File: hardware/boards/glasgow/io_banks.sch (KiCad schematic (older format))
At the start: 21 parts, among them J10 Conn_01x03, J4 Conn_01x02, J5 Conn_02x22_Odd_Even, U30 ICE40HX8K-BG121, U32 SN74LVC1T45DRL

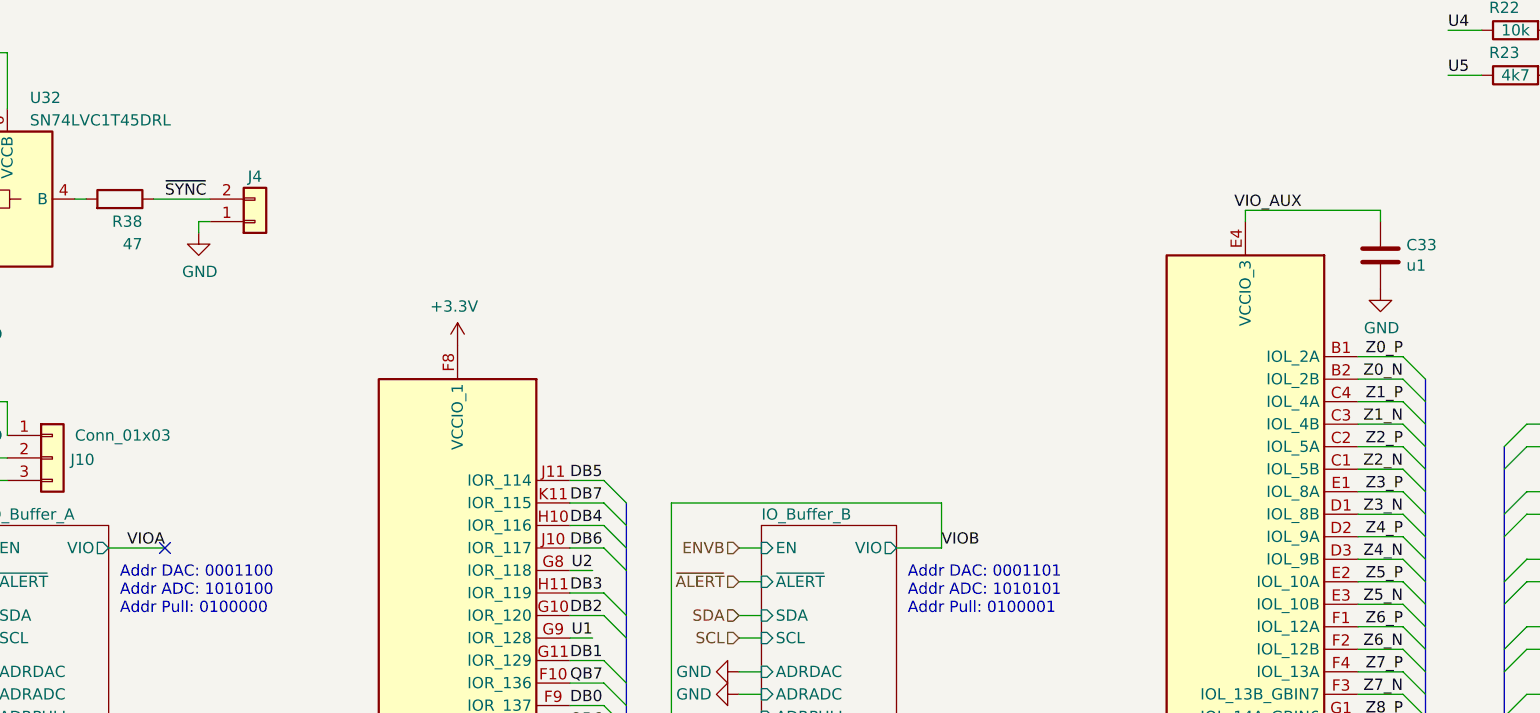
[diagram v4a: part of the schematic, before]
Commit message: revC1: fix some ERC errors
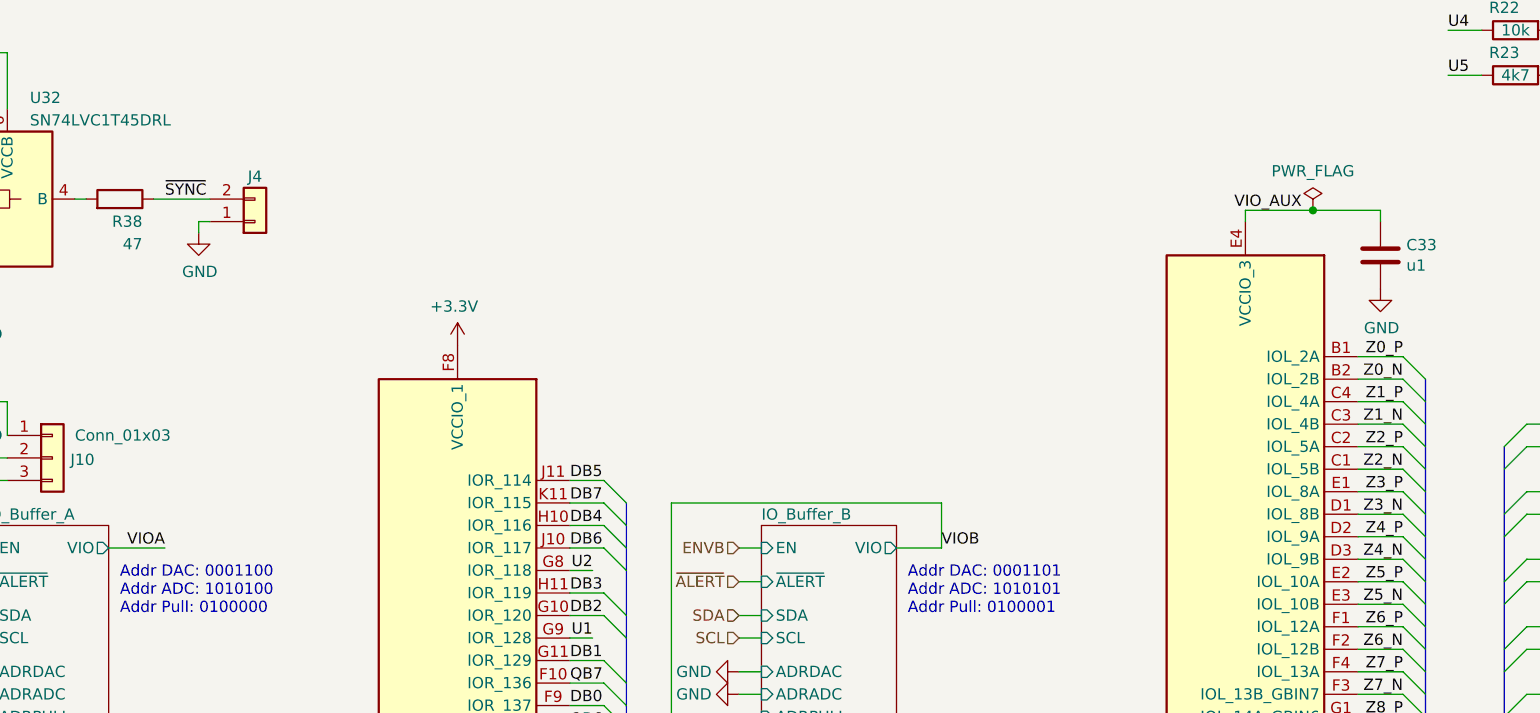
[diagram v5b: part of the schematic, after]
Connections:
- no-connect marks 3 -> 2
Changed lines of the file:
@@
 Text Label 3450 3950 2    50   ~ 0
 VIOA
-NoConn ~ 3450 3950
 Wire Wire Line
 	3200 3950 3450 3950
@@
 $EndComp
 Wire Wire Line
-	8250 2450 8850 2450
+	8250 2450 8550 2450
 Connection ~ 2400 5800
 Connection ~ 5850 5800
@@
 Wire Bus Line
 	9050 3200 9050 5800
+$Comp
+L power:PWR_FLAG #FLG0101
+U 1 1 5CFF6FB6
+P 8550 2450
+F 0 "#FLG0101" H 8550 2525 50  0001 C CNN
+F 1 "PWR_FLAG" H 8550 2624 50  0000 C CNN
+F 2 "" H 8550 2450 50  0001 C CNN
+F 3 "~" H 8550 2450 50  0001 C CNN
+	1    8550 2450
+	1    0    0    -1
+$EndComp
+Connection ~ 8550 2450
+Wire Wire Line
+	8550 2450 8850 2450
 $EndSCHEMATC

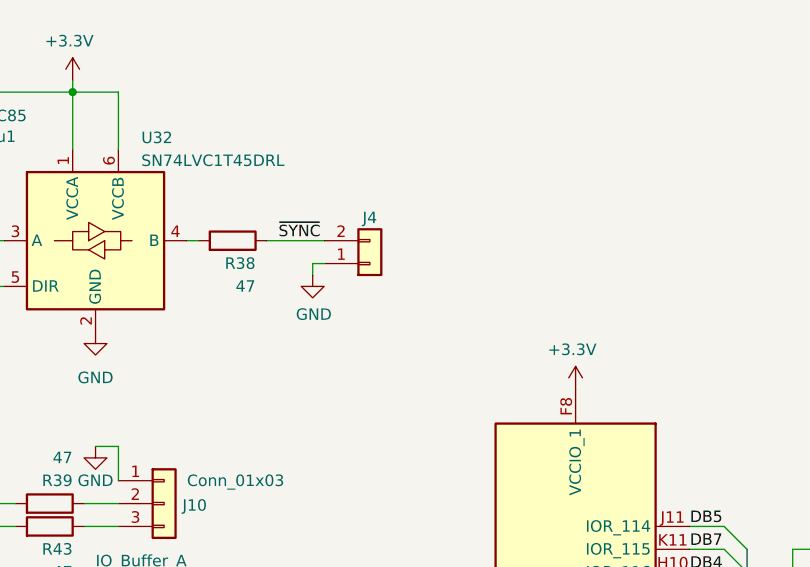
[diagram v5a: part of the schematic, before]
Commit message: revC1: add a TVS protection diode to SYNC
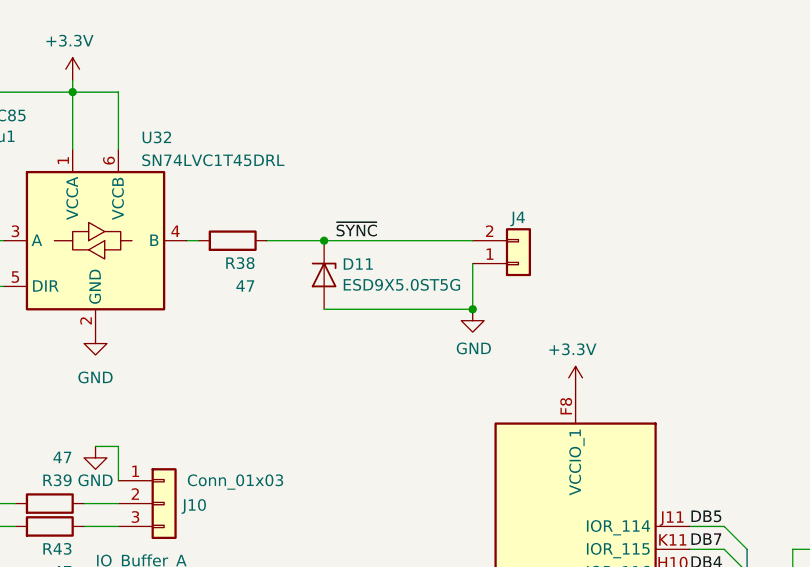
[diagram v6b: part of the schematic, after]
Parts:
- added D11: ESD9X5.0ST5G, Diode_SMD:D_0402_1005Metric, symbol Device:D_Zener
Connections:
- net GND: now also D11.2 (A)
- net ~SYNC: now also D11.1 (K)
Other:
- moved on the sheet: J4
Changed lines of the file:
@@
 L Connector_Generic:Conn_01x02 J?
 U 1 1 5C961091
-P 3850 2500
+P 4500 2500
 AR Path="/5C961091" Ref="J?"  Part="1"
 AR Path="/5C7B59B0/5C961091" Ref="J4"  Part="1"
-F 0 "J4" H 3850 2300 50  0000 C CNN
-F 1 "Conn_01x02" H 3930 2401 50  0001 L CNN
-F 2 "Connector_PinHeader_2.54mm:PinHeader_1x02_P2.54mm_Horizontal" H 3850 2500 50  0001 C CNN
-F 3 "https://www.mouser.hk/datasheet/2/418/NG_CD_640455_Y3-1255934.pdf" H 3850 2500 50  0001 C CNN
-F 4 "Molex" H -6750 -350 50  0001 C CNN "Mfg"
-F 5 "22-05-3021" H -6750 -350 50  0001 C CNN "MPN"
-	1    3850 2500
+F 0 "J4" H 4500 2300 50  0000 C CNN
+F 1 "Conn_01x02" H 4580 2401 50  0001 L CNN
+F 2 "Connector_PinHeader_2.54mm:PinHeader_1x02_P2.54mm_Horizontal" H 4500 2500 50  0001 C CNN
+F 3 "https://www.mouser.hk/datasheet/2/418/NG_CD_640455_Y3-1255934.pdf" H 4500 2500 50  0001 C CNN
+F 4 "Molex" H -6100 -350 50  0001 C CNN "Mfg"
+F 5 "22-05-3021" H -6100 -350 50  0001 C CNN "MPN"
+	1    4500 2500
 	1    0    0    1
 $EndComp
@@
 L power:GND #PWR?
 U 1 1 5C961098
-P 3600 2550
+P 4300 2700
 AR Path="/5C961098" Ref="#PWR?"  Part="1"
 AR Path="/5C7B59B0/5C961098" Ref="#PWR042"  Part="1"
-F 0 "#PWR042" H 3600 2300 50  0001 C CNN
-F 1 "GND" H 3605 2377 50  0000 C CNN
-F 2 "" H 3600 2550 50  0001 C CNN
-F 3 "" H 3600 2550 50  0001 C CNN
-	1    3600 2550
-	1    0    0    -1
-$EndComp
-Wire Wire Line
-	3650 2500 3600 2500
-Wire Wire Line
-	3600 2500 3600 2550
-Text Label 3450 2400 0    50   ~ 0
+F 0 "#PWR042" H 4300 2450 50  0001 C CNN
+F 1 "GND" H 4305 2527 50  0000 C CNN
+F 2 "" H 4300 2700 50  0001 C CNN
+F 3 "" H 4300 2700 50  0001 C CNN
+	1    4300 2700
+	1    0    0    -1
+$EndComp
+Text Label 3700 2400 0    50   ~ 0
 ~SYNC
 $Comp
@@
 Wire Wire Line
 	2750 3300 2750 3450
-Wire Bus Line
-	2400 4950 2400 5800
-Wire Bus Line
-	3450 4950 3450 5800
-Wire Bus Line
-	6950 4950 6950 5800
-Wire Bus Line
-	5850 4950 5850 5800
-Wire Bus Line
-	10650 3700 10650 5800
-Wire Bus Line
-	9400 3500 9400 5800
-Wire Bus Line
-	2050 3850 2050 5800
-Wire Bus Line
-	5500 3750 5500 5800
-Wire Bus Line
-	9050 3200 9050 5800
 $Comp
 L power:PWR_FLAG #FLG0101
@@
 Wire Wire Line
 	8550 2450 8850 2450
+$Comp
+L Device:D_Zener D11
+U 1 1 5D1DFDD1
+P 3650 2550
+F 0 "D11" V 3604 2629 50  0000 L CNN
+F 1 "ESD9X5.0ST5G" V 3695 2629 50  0000 L CNN
+F 2 "Diode_SMD:D_0402_1005Metric" H 3650 2550 50  0001 C CNN
+F 3 "https://www.onsemi.com/pub/Collateral/ESD9X3.3ST5G-D.PDF" H 3650 2550 50  0001 C CNN
+	1    3650 2550
+	0    1    1    0
+$EndComp
+Connection ~ 3650 2400
+Wire Wire Line
+	4300 2500 4300 2700
+Connection ~ 4300 2700
+Wire Wire Line
+	3650 2400 4300 2400
+Wire Wire Line
+	3650 2700 4300 2700
+Wire Bus Line
+	2400 4950 2400 5800
+Wire Bus Line
+	3450 4950 3450 5800
+Wire Bus Line
+	6950 4950 6950 5800
+Wire Bus Line
+	5850 4950 5850 5800
+Wire Bus Line
+	10650 3700 10650 5800
+Wire Bus Line
+	9400 3500 9400 5800
+Wire Bus Line
+	2050 3850 2050 5800
+Wire Bus Line
+	5500 3750 5500 5800
+Wire Bus Line
+	9050 3200 9050 5800
 $EndSCHEMATC

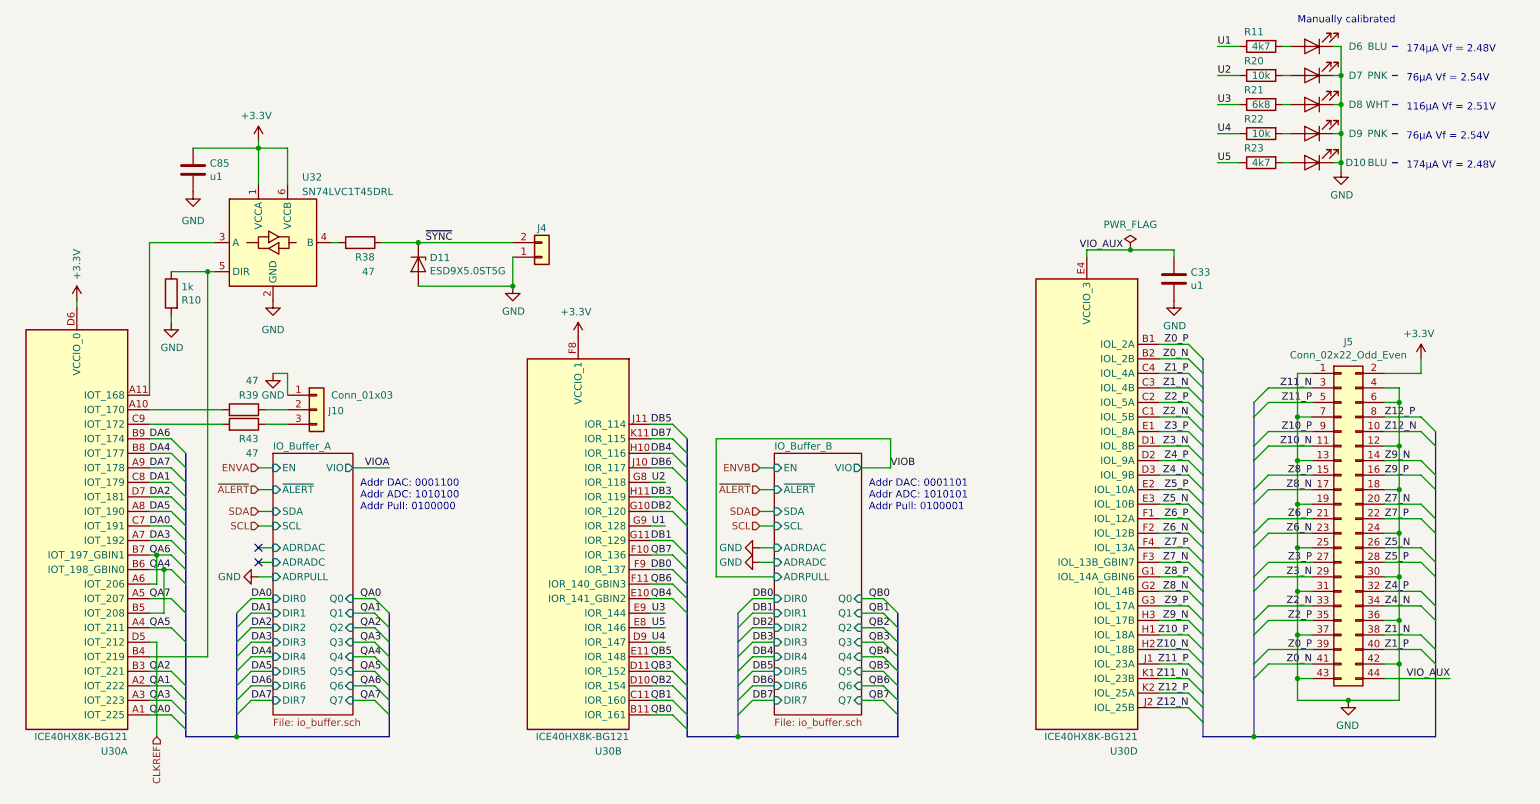
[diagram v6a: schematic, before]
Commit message: revC: tiny changes to text placement on schematic for readability.
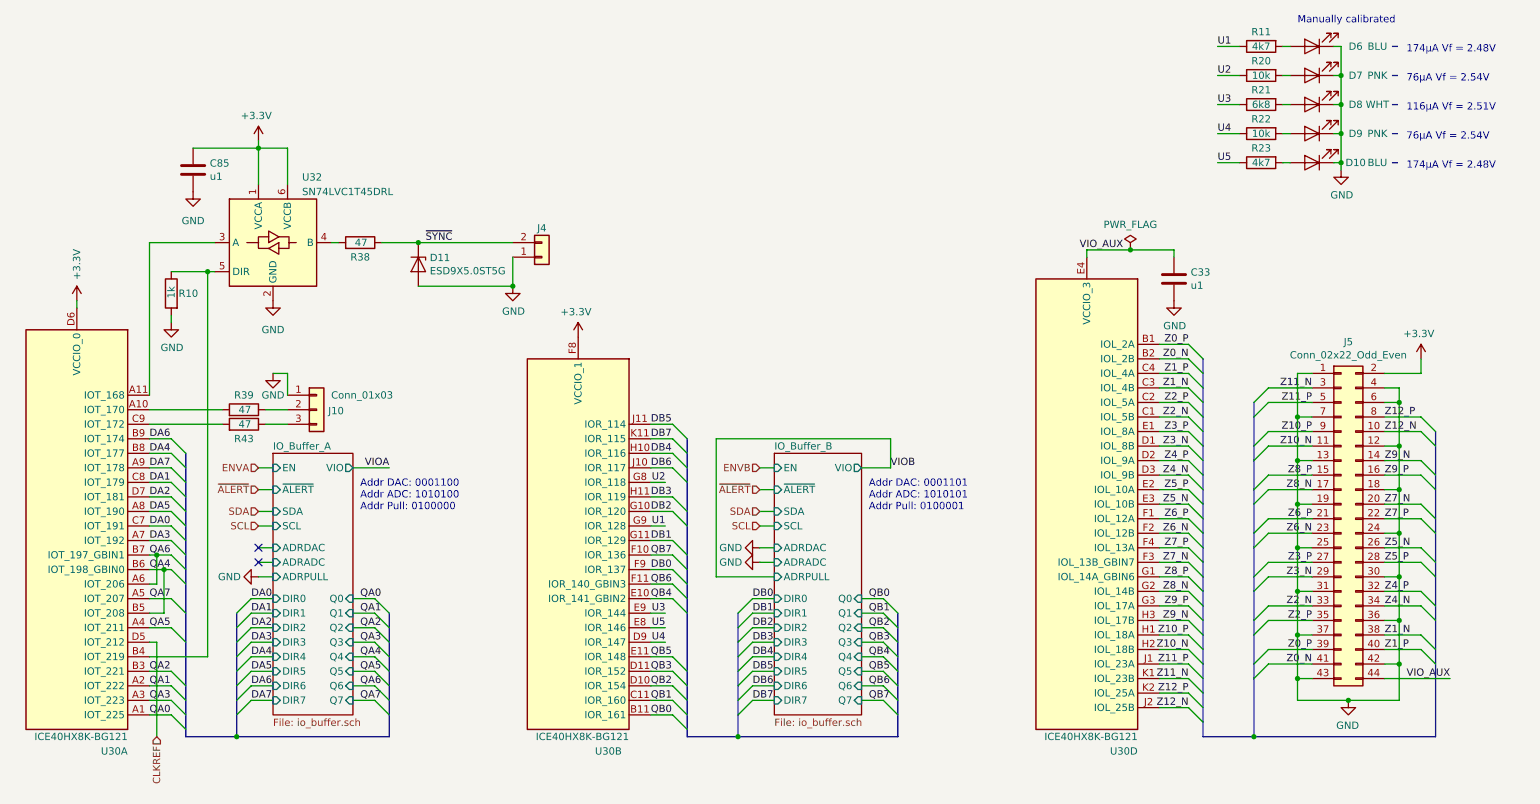
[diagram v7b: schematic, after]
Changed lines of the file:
@@
 EESchema Schematic File Version 4
 LIBS:glasgow-cache
-EELAYER 26 0
+EELAYER 29 0
 EELAYER END
 $Descr A4 11693 8268
@@
 AR Path="/5C9E34D0" Ref="R?"  Part="1"
 AR Path="/5C7B59B0/5C9E34D0" Ref="R11"  Part="1"
-F 0 "R11" V 9350 1100 50  0000 C CNN
+F 0 "R11" V 9350 1050 50  0000 C CNN
 F 1 "4k7" V 9450 1050 50  0000 C CNN
 F 2 "Resistor_SMD:R_0402_1005Metric" V 9380 1050 50  0001 C CNN
@@
 AR Path="/5C9E34DB" Ref="R?"  Part="1"
 AR Path="/5C7B59B0/5C9E34DB" Ref="R22"  Part="1"
-F 0 "R22" V 9350 1700 50  0000 C CNN
+F 0 "R22" V 9350 1650 50  0000 C CNN
 F 1 "10k" V 9450 1650 50  0000 C CNN
 F 2 "Resistor_SMD:R_0402_1005Metric" V 9380 1650 50  0001 C CNN
@@
 AR Path="/5C9E34EB" Ref="R?"  Part="1"
 AR Path="/5C7B59B0/5C9E34EB" Ref="R23"  Part="1"
-F 0 "R23" V 9350 1900 50  0000 C CNN
+F 0 "R23" V 9350 1850 50  0000 C CNN
 F 1 "4k7" V 9450 1850 50  0000 C CNN
 F 2 "Resistor_SMD:R_0402_1005Metric" V 9380 1850 50  0001 C CNN
@@
 AR Path="/5C9E34F4" Ref="R?"  Part="1"
 AR Path="/5C7B59B0/5C9E34F4" Ref="R20"  Part="1"
-F 0 "R20" V 9350 1300 50  0000 C CNN
+F 0 "R20" V 9350 1250 50  0000 C CNN
 F 1 "10k" V 9450 1250 50  0000 C CNN
 F 2 "Resistor_SMD:R_0402_1005Metric" V 9380 1250 50  0001 C CNN
@@
 AR Path="/5C9E34FD" Ref="R?"  Part="1"
 AR Path="/5C7B59B0/5C9E34FD" Ref="R21"  Part="1"
-F 0 "R21" V 9350 1500 50  0000 C CNN
+F 0 "R21" V 9350 1450 50  0000 C CNN
 F 1 "6k8" V 9450 1450 50  0000 C CNN
 F 2 "Resistor_SMD:R_0402_1005Metric" V 9380 1450 50  0001 C CNN
@@
 AR Path="/5C9610A4" Ref="R?"  Part="1"
 AR Path="/5C7B59B0/5C9610A4" Ref="R10"  Part="1"
-F 0 "R10" H 1880 2704 50  0000 R CNN
-F 1 "1k" H 1880 2795 50  0000 R CNN
+F 0 "R10" H 1900 2750 50  0000 R CNN
+F 1 "1k" V 1950 2800 50  0000 R CNN
 F 2 "Resistor_SMD:R_0402_1005Metric" V 1880 2750 50  0001 C CNN
 F 3 "https://www.mouser.com/datasheet/2/447/PYu-AC_51_RoHS_L_6-1152827.pdf" H 1950 2750 50  0001 C CNN
@@
 AR Path="/5CBF4EC8" Ref="R?"  Part="1"
 AR Path="/5C7B59B0/5CBF4EC8" Ref="R38"  Part="1"
-F 0 "R38" V 3150 2500 50  0000 R CNN
-F 1 "47" V 3050 2500 50  0000 R CNN
+F 0 "R38" V 3150 2400 50  0000 C CNN
+F 1 "47" V 3250 2450 50  0000 R CNN
 F 2 "Resistor_SMD:R_0402_1005Metric" V 3180 2400 50  0001 C CNN
 F 3 "https://www.mouser.com/datasheet/2/447/PYu-AC_51_RoHS_L_6-1152827.pdf" H 3250 2400 50  0001 C CNN
@@
 AR Path="/5CBF658E" Ref="R?"  Part="1"
 AR Path="/5C7B59B0/5CBF658E" Ref="R39"  Part="1"
-F 0 "R39" V 2550 3650 50  0000 R CNN
-F 1 "47" V 2650 3650 50  0000 R CNN
+F 0 "R39" V 2550 3550 50  0000 C CNN
+F 1 "47" V 2450 3600 50  0000 R CNN
 F 2 "Resistor_SMD:R_0402_1005Metric" V 2380 3550 50  0001 C CNN
 F 3 "https://www.mouser.com/datasheet/2/447/PYu-AC_51_RoHS_L_6-1152827.pdf" H 2450 3550 50  0001 C CNN
@@
 AR Path="/5CBF65F8" Ref="R?"  Part="1"
 AR Path="/5C7B59B0/5CBF65F8" Ref="R43"  Part="1"
-F 0 "R43" V 2350 3750 50  0000 R CNN
-F 1 "47" V 2250 3750 50  0000 R CNN
+F 0 "R43" V 2350 3650 50  0000 C CNN
+F 1 "47" V 2450 3700 50  0000 R CNN
 F 2 "Resistor_SMD:R_0402_1005Metric" V 2380 3650 50  0001 C CNN
 F 3 "https://www.mouser.com/datasheet/2/447/PYu-AC_51_RoHS_L_6-1152827.pdf" H 2450 3650 50  0001 C CNN

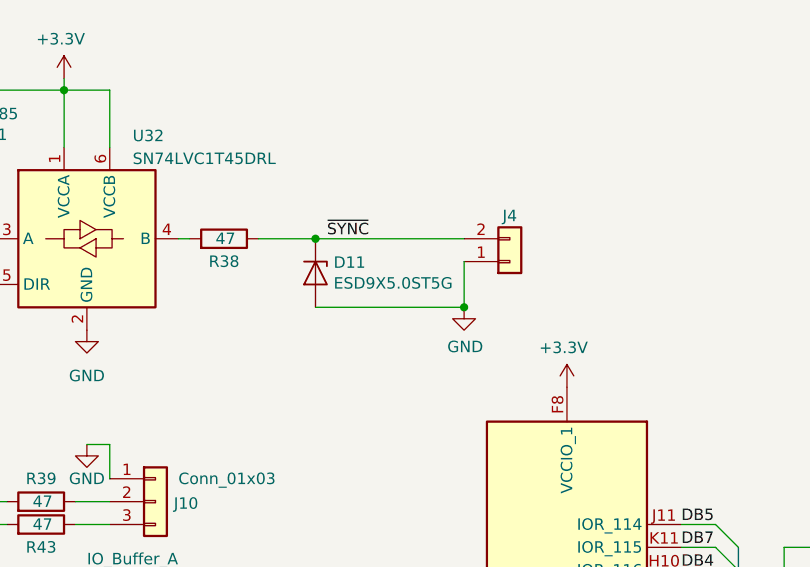
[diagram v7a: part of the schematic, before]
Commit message: revC1: switch to a SOD-523 diode for the SYNC protection
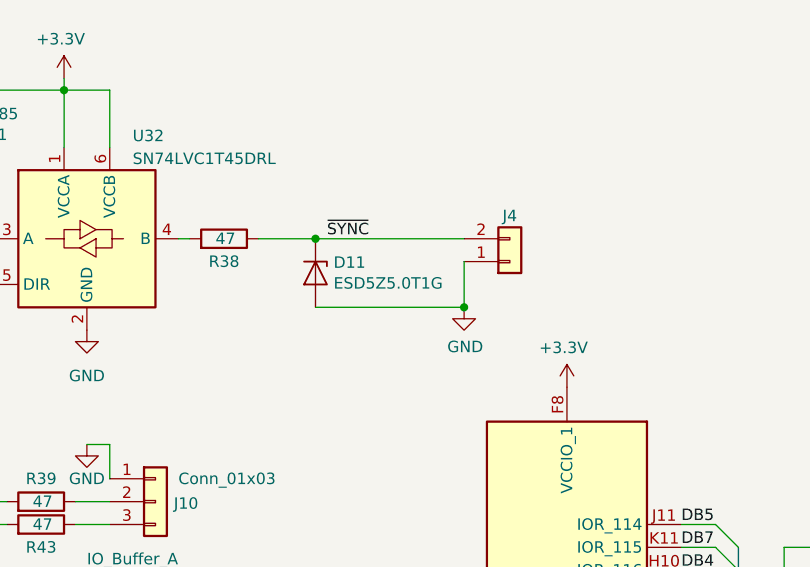
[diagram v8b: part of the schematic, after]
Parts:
- D11: value ESD9X5.0ST5G -> ESD5Z5.0T1G; footprint Diode_SMD:D_0402_1005Metric -> Diode_SMD:D_SOD-523
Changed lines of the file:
@@
 P 3650 2550
 F 0 "D11" V 3604 2629 50  0000 L CNN
-F 1 "ESD9X5.0ST5G" V 3695 2629 50  0000 L CNN
-F 2 "Diode_SMD:D_0402_1005Metric" H 3650 2550 50  0001 C CNN
-F 3 "https://www.onsemi.com/pub/Collateral/ESD9X3.3ST5G-D.PDF" H 3650 2550 50  0001 C CNN
+F 1 "ESD5Z5.0T1G" V 3695 2629 50  0000 L CNN
+F 2 "Diode_SMD:D_SOD-523" H 3650 2550 50  0001 C CNN
+F 3 "https://www.onsemi.com/pub/Collateral/ESD5Z2.5T1-D.PDF" H 3650 2550 50  0001 C CNN
 	1    3650 2550
 	0    1    1    0
